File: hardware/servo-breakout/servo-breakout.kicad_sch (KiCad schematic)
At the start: 18 parts, among them J1 Servos 1-4, J2 Servos 5-8, M1 Servo 1, M2 Servo 2, M3 Servo 3, M4 Servo 4, M5 Servo 5, M6 Servo 6, M7 Servo 7, M8 Servo 8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

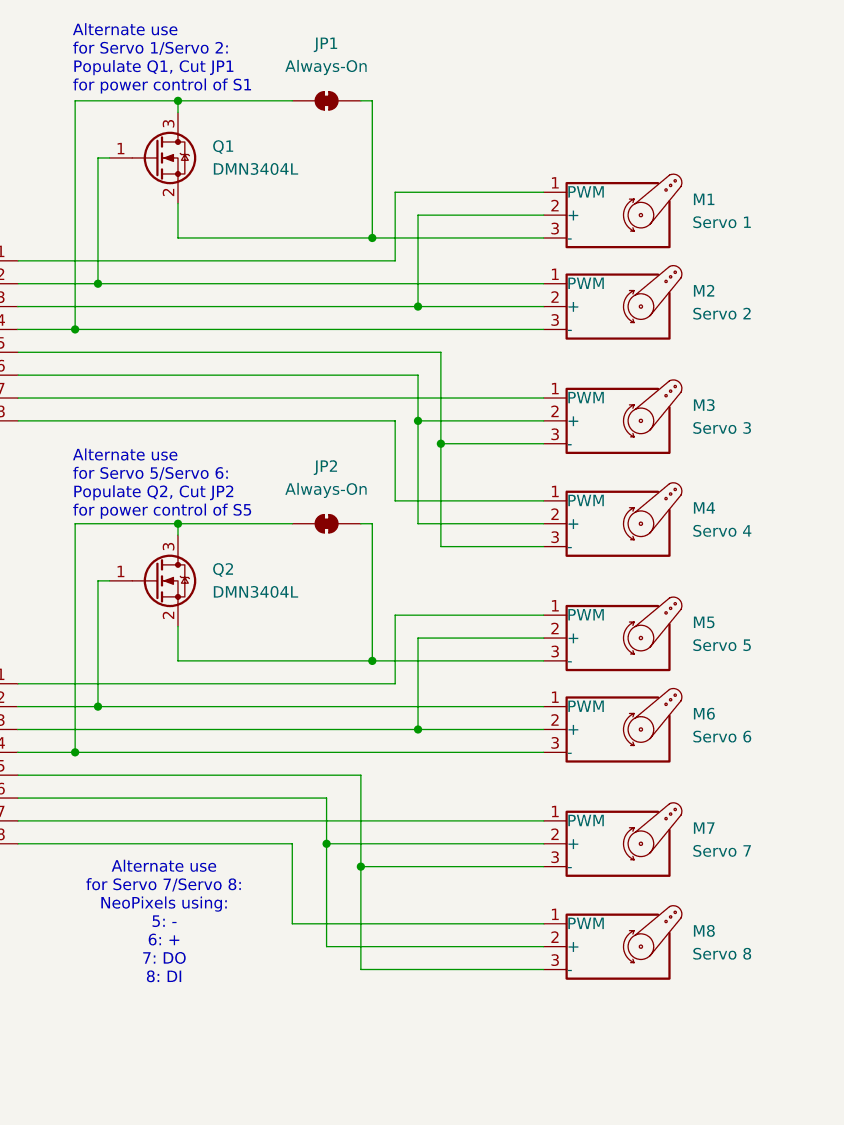
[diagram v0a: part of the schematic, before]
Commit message: Rev 1.1: - Update to latest KiCad - Fixed short in servo board - Updates to right-angle diag connector on servo boards - Fixed microproc footprint on diag board - Flipped I2C connector to top of diag board - Pass all ERC and DRC checks, add exclusions
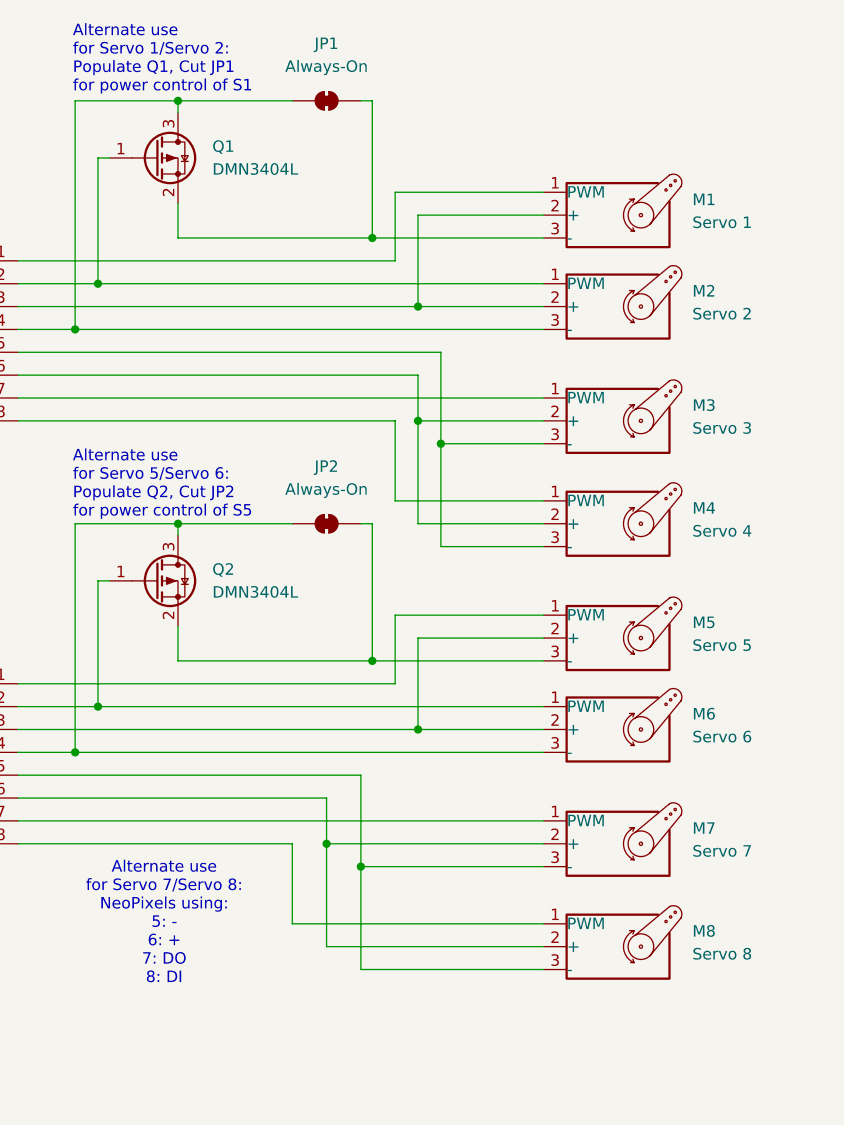
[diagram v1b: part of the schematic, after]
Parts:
- Q1, Q2: symbol Device:Q_NMOS_GSD -> Transistor_FET:Q_PMOS_GSD
